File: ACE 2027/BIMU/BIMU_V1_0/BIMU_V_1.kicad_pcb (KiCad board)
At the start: 2 copper layers, 35 x 40.5 mm, 53 parts, among them J201 UART_connector, J202 USB_C_Receptacle_USB2.0_16P, J203 RJ45, J204 RJ45, SW201 SW_Push, SW202 SW_Push, U101 AP7361C-33E, U201 ESP32-C3, U202 SN65HVD232DR, U301 LSM6DSV16BXTR, Y201 ABM8-40.000MHZ-10-D1G-T

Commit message: Avancement du pcb layout
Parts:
- TP101, TP102, TP103, TP201, TP202: footprint Connector_PinHeader_2.54mm:PinHeader_1x01_P2.54mm_Vertical -> TestPoint:TestPoint_Pad_1.0x1.0mm

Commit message: Avancement placement des composants
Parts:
- C301, C302, R101, R209, R210, U202: moved to B.Cu
- moved C101 165.7 mm to (232.4, 55.6)
- moved R210 129.8 mm to (205.1, 62.6), turned to 180 degrees
- moved R209 129.7 mm to (205.1, 58.5), turned to 180 degrees
- moved R101 125.2 mm to (205.1, 54.4), turned to 180 degrees
- moved C206 110.3 mm to (178.9, 76.9), turned to -90 degrees
- moved C207 103.1 mm to (172.1, 76.9), turned to 90 degrees
- moved C102 100.0 mm to (163.8, 58.5)
- moved R208 97.8 mm to (164.4, 89.7)
- moved C302 97.2 mm to (193.4, 71.0), turned to 180 degrees
- moved C204 96.7 mm to (160.8, 84.4)
- moved R207 94.1 mm to (157.9, 91.4)
- moved C301 91.1 mm to (187.7, 73.1), turned to 180 degrees
- moved H102 91.1 mm to (206.1, 84.5)
- moved C205 87.9 mm to (151.4, 86.9)
- moved C201 85.8 mm to (156.5, 42.9)
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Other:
- board size 35 x 40.5 mm -> 40 x 35 mm
- board text added: "MASTER"

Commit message: avancement
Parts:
- moved C102 3.64 mm to (160.7, 56.6)
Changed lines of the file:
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@@
 	(footprint "Capacitor_SMD:C_0805_2012Metric_Pad1.18x1.45mm_HandSolder"
 		(layer "F.Cu")
-		(at 163.8 58.5)
+		(at 160.7 56.6)
 		(descr "Capacitor SMD 0805 (2012 Metric), square (rectangular) end terminal, IPC-7351 nominal with elongated pad for handsoldering. (Body size source: IPC-SM-782 page 76, https://www.pcb-3d.com/wordpress/wp-content/uploads/ipc-sm-782a_amendment_1_and_2.pdf, https://docs.google.com/spreadsheets/d/1BsfQQcO9C6DZCsRaXUlFlo91Tg2WpOkGARC1WS5S8t0/edit?usp=sharing), generated with kicad-footprint-generator")
 		(tags "capacitor handsolder")

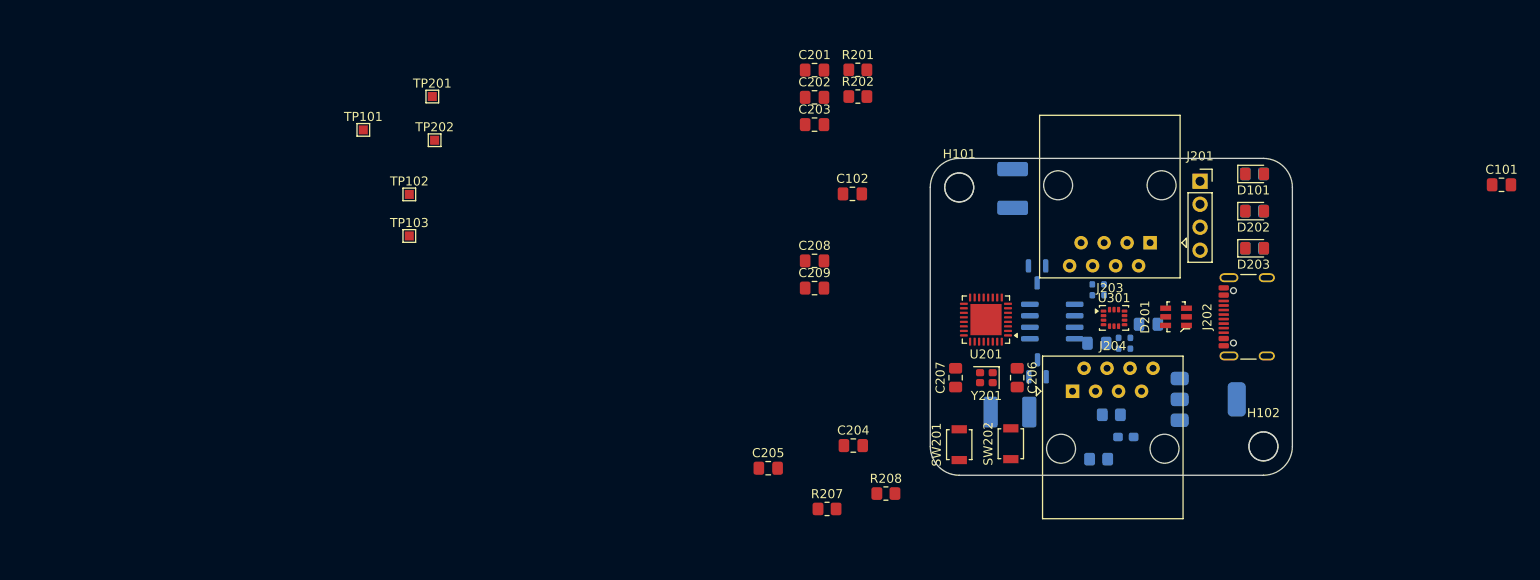
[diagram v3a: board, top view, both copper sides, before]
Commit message: Finaliser le placement des composants  et routé le CAN différentiel
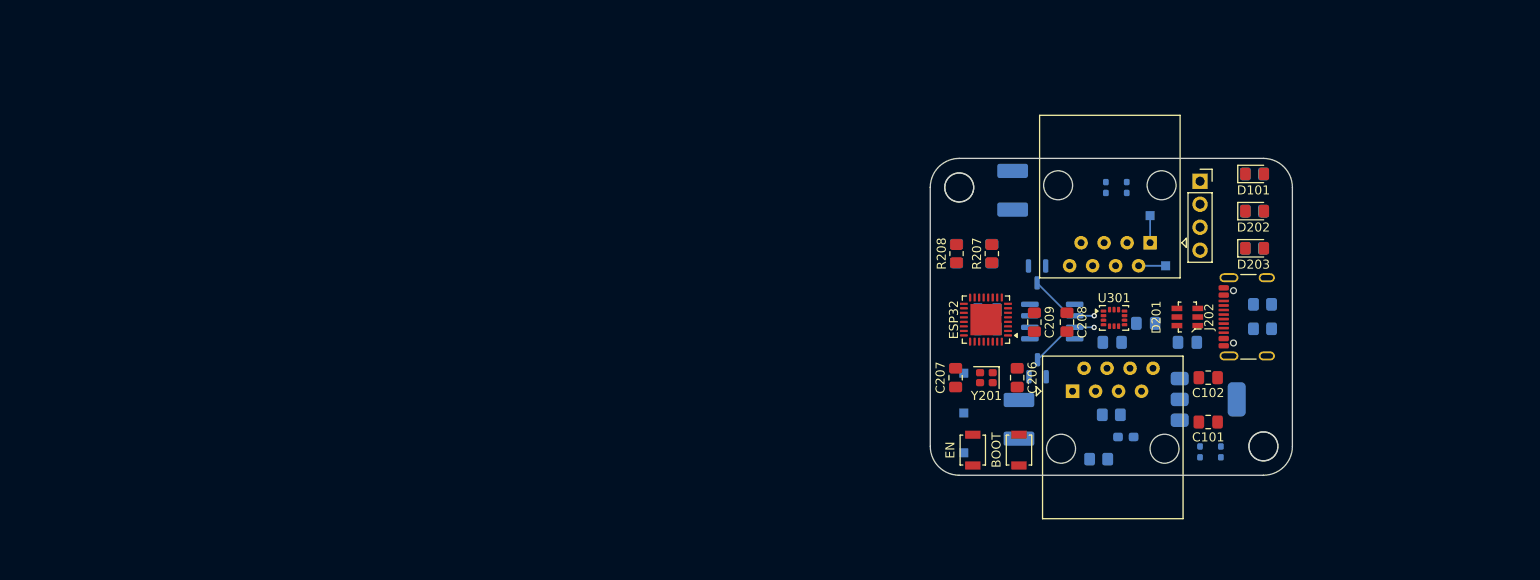
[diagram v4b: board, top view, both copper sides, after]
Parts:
- C201, C202, C203, C204, C205, R201, R202: moved to B.Cu
- TP_3.3V: renamed from TP103; moved to B.Cu
- TP_5V: renamed from TP102; moved to B.Cu
- TP_CAN_N: renamed from TP202; moved to B.Cu
- TP_CAN_P: renamed from TP201; moved to B.Cu
- TP_GND: renamed from TP101; moved to B.Cu
- moved TP_CAN_N 81.9 mm to (195.3, 64.5)
- moved TP_CAN_P 80.4 mm to (193.6, 59.0)
- moved TP_GND 73.3 mm to (173.0, 80.8)
- moved TP_3.3V 65.8 mm to (173.0, 85.2)
- moved TP_5V 64.3 mm to (173.0, 76.4)
- moved R201 53.1 mm to (206.0, 71.5)
- moved R202 50.2 mm to (206.0, 68.8)
- moved C203 47.7 mm to (197.7, 73.0), turned to 180 degrees
- moved C102 44.2 mm to (200.0, 76.9), turned to 180 degrees
- moved C101 41.7 mm to (200.0, 81.8), turned to 180 degrees
- moved C205 34.2 mm to (176.1, 63.2), turned to 90 degrees
- moved R207 33.6 mm to (176.1, 63.2), turned to 90 degrees
- moved C201 32.6 mm to (175.6, 69.4), turned to 180 degrees
- moved C202 31.9 mm to (175.6, 71.5), turned to 180 degrees
- moved C208 28.7 mm to (184.4, 70.8), turned to -90 degrees
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- renumbered SW202 to BOOT, SW201 to EN, U201 to ESP32
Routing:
- net CAN_P: track 0.00 -> 30.8 mm, vias 0 -> 1
- net CAN_N: track 0.00 -> 30.8 mm, vias 0 -> 1
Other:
- copper layers 2 -> 4
- board text added: "ETH-UART"

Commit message: Avancement de la puissance
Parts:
- moved TP_5V 16.5 mm to (179.5, 61.3)
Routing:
- net +5V: track 0.00 -> 63.5 mm, vias 0 -> 8
- added copper zone on In1.Cu, net +3.3V
- added copper zone on In2.Cu, net GND

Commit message: Traceage des pistes du PCB bientot complété
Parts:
- turned R101 to 0 degrees
- renumbered D202 to CONNECTED, D203 to ERROR, D101 to POWER
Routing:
- net U0RX: track 0.00 -> 89.6 mm
- net U0TX: track 0.00 -> 86.5 mm, vias 0 -> 2
- net GND: track 0.00 -> 52.3 mm, vias 0 -> 49
- net +3.3V: track 0.00 -> 38.4 mm, vias 0 -> 27
- net CONNECTED LED: track 0.00 -> 36.1 mm, vias 0 -> 3
- net EN: track 0.00 -> 32.4 mm, vias 0 -> 3
- net BOOT: track 0.00 -> 30.5 mm, vias 0 -> 5
- net ERROR_LED: track 0.00 -> 30.3 mm, vias 0 -> 3
- net USB_D+: track 0.00 -> 26.0 mm, vias 0 -> 4
- net USB_D-: track 0.00 -> 25.7 mm, vias 0 -> 4
- net CS: track 0.00 -> 20.1 mm
- net I2C_SDA: track 0.00 -> 19.5 mm, vias 0 -> 2
- net MOSI: track 0.00 -> 16.4 mm
- net SCLK: track 0.00 -> 16.1 mm, vias 0 -> 2
- net Net-(J204-Pad6): track 0.00 -> 16.0 mm, vias 0 -> 1
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
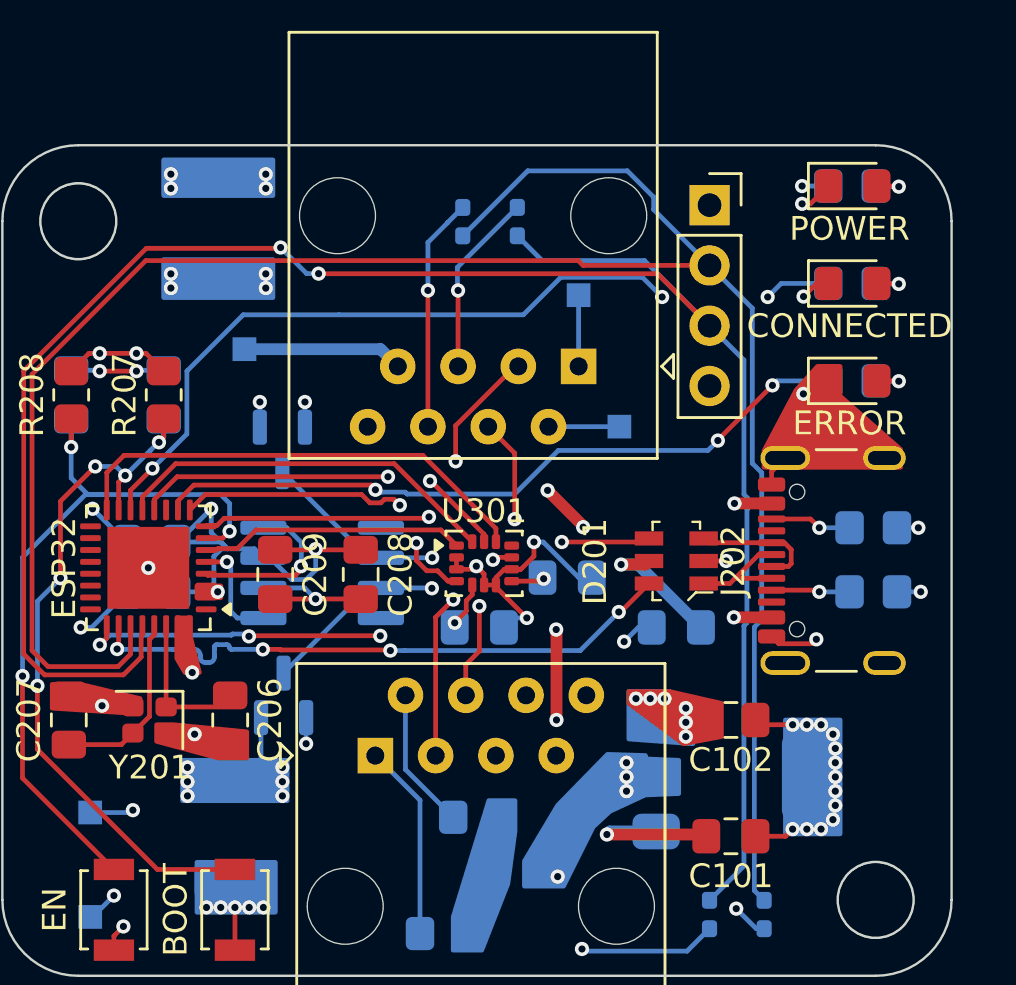
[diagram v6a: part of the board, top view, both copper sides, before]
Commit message: Amélioration silkscreen
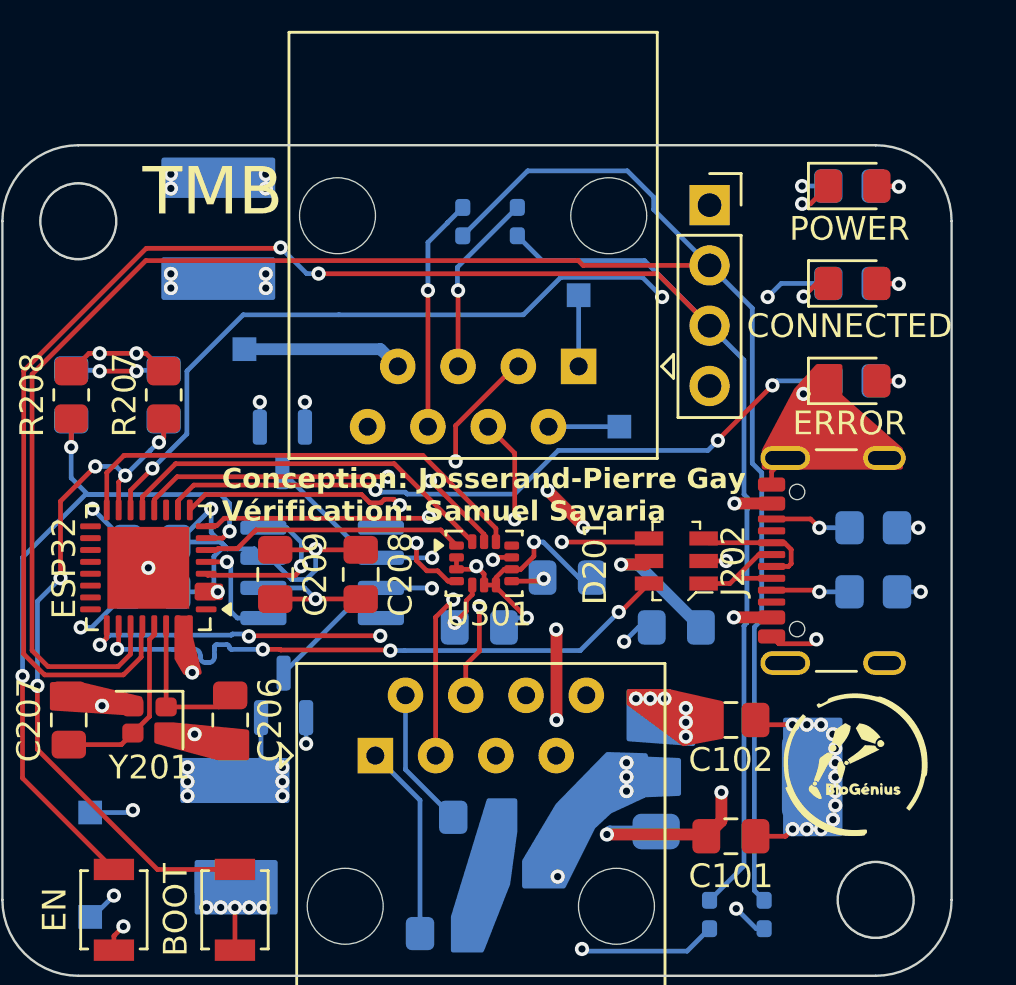
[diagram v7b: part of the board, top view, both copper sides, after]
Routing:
- net +5V: track 63.5 -> 73.2 mm, vias 8 -> 9
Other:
- board text added: "Conception: Josserand-Pierre Gay Vérification: Samuel Savaria"
- board text added: "TMB"
